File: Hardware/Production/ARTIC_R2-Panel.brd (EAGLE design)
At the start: 113 x 122.2 mm, 1045 parts, among them J1 U.FL, J10 U.FL, J11 THING_PLUS, J12 U.FL, J13 THING_PLUS, J14 U.FL, J15 THING_PLUS, J16 U.FL, J2 THING_PLUS, J3 THING_PLUS, J4 U.FL, J5 THING_PLUS, J6 U.FL, J7 THING_PLUS, J8 U.FL, J9 THING_PLUS, Q1 20V/4.2A/52mΩ/1.4W, Q2 20V/4.2A/52mΩ/1.4W, Q3 20V/4.2A/52mΩ/1.4W, Q4 20V/4.2A/52mΩ/1.4W, Q5 20V/4.2A/52mΩ/1.4W, Q6 20V/4.2A/52mΩ/1.4W, Q7 20V/4.2A/52mΩ/1.4W, Q8 20V/4.2A/52mΩ/1.4W, U1 32M SPI Flash, U10 1.8V/100mA, U11 32M SPI Flash, U12 DUAL-OPTOISOLATOR_SOIC8, U13 ARTIC_R2, U14 RFPA0133, U15 AS179-92LF, U16 1.8V/100mA, U17 32M SPI Flash, U18 DUAL-OPTOISOLATOR_SOIC8, U19 ARTIC_R2, U2 1.8V/100mA, U20 RFPA0133, U21 AS179-92LF, U22 1.8V/100mA, U23 32M SPI Flash, U24 DUAL-OPTOISOLATOR_SOIC8, U25 ARTIC_R2, U26 RFPA0133, U27 AS179-92LF, U28 1.8V/100mA, U29 32M SPI Flash, U3 ARTIC_R2, U30 DUAL-OPTOISOLATOR_SOIC8, U31 ARTIC_R2, U32 RFPA0133, U33 AS179-92LF, U34 1.8V/100mA, U35 32M SPI Flash, U36 DUAL-OPTOISOLATOR_SOIC8, U37 ARTIC_R2, U38 RFPA0133, U39 AS179-92LF, U4 RFPA0133, U40 1.8V/100mA, U41 32M SPI Flash, U42 DUAL-OPTOISOLATOR_SOIC8, U43 ARTIC_R2, U44 RFPA0133, U45 AS179-92LF, U46 1.8V/100mA, U47 32M SPI Flash, U48 DUAL-OPTOISOLATOR_SOIC8, U5 AS179-92LF, U6 DUAL-OPTOISOLATOR_SOIC8, U7 ARTIC_R2, U8 RFPA0133, U9 AS179-92LF, X1 CRYSTAL-TCXO-26MHZ, X2 CRYSTAL-TCXO-26MHZ, X3 CRYSTAL-TCXO-26MHZ, X4 CRYSTAL-TCXO-26MHZ, X5 CRYSTAL-TCXO-26MHZ, X6 CRYSTAL-TCXO-26MHZ, X7 CRYSTAL-TCXO-26MHZ, X8 CRYSTAL-TCXO-26MHZ

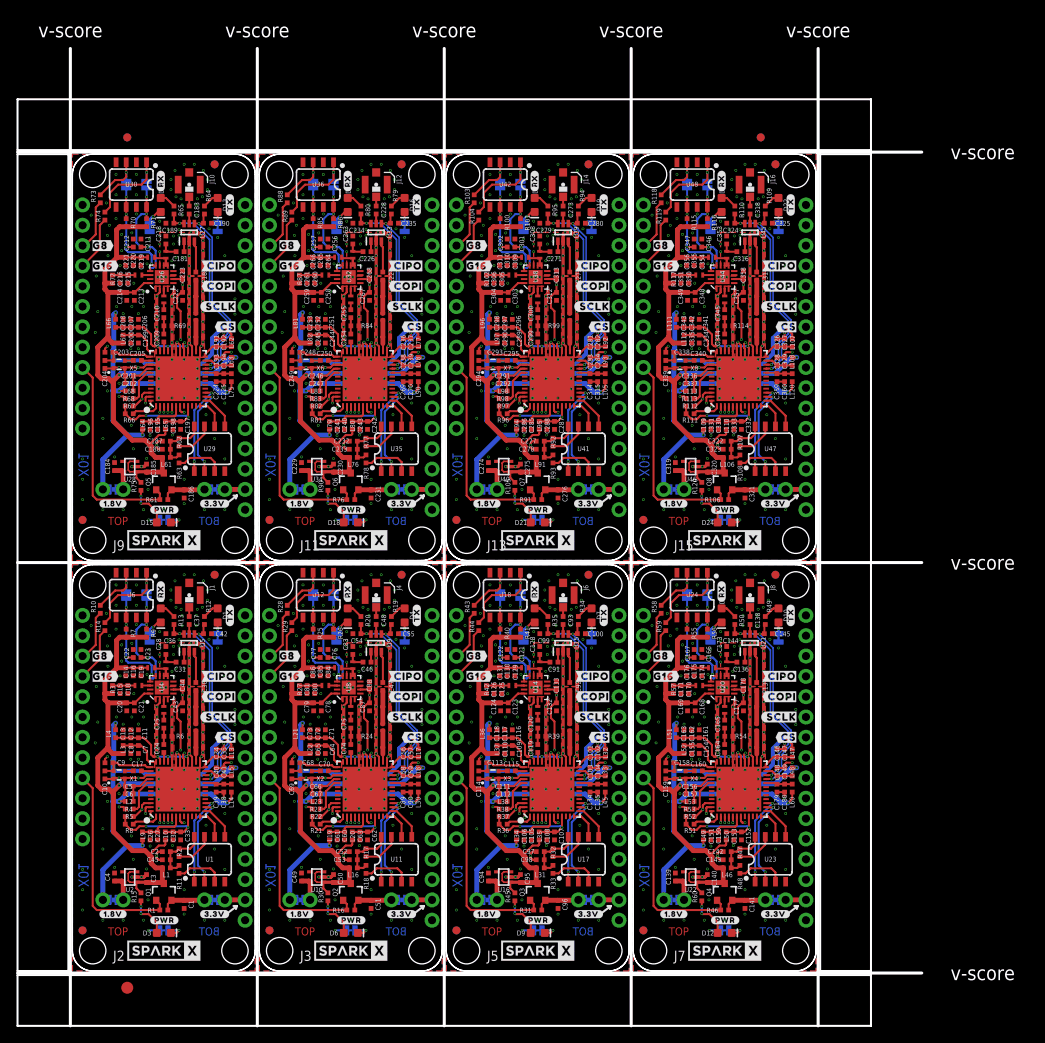
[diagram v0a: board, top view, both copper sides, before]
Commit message: ).8mm PCB with Impedance Control
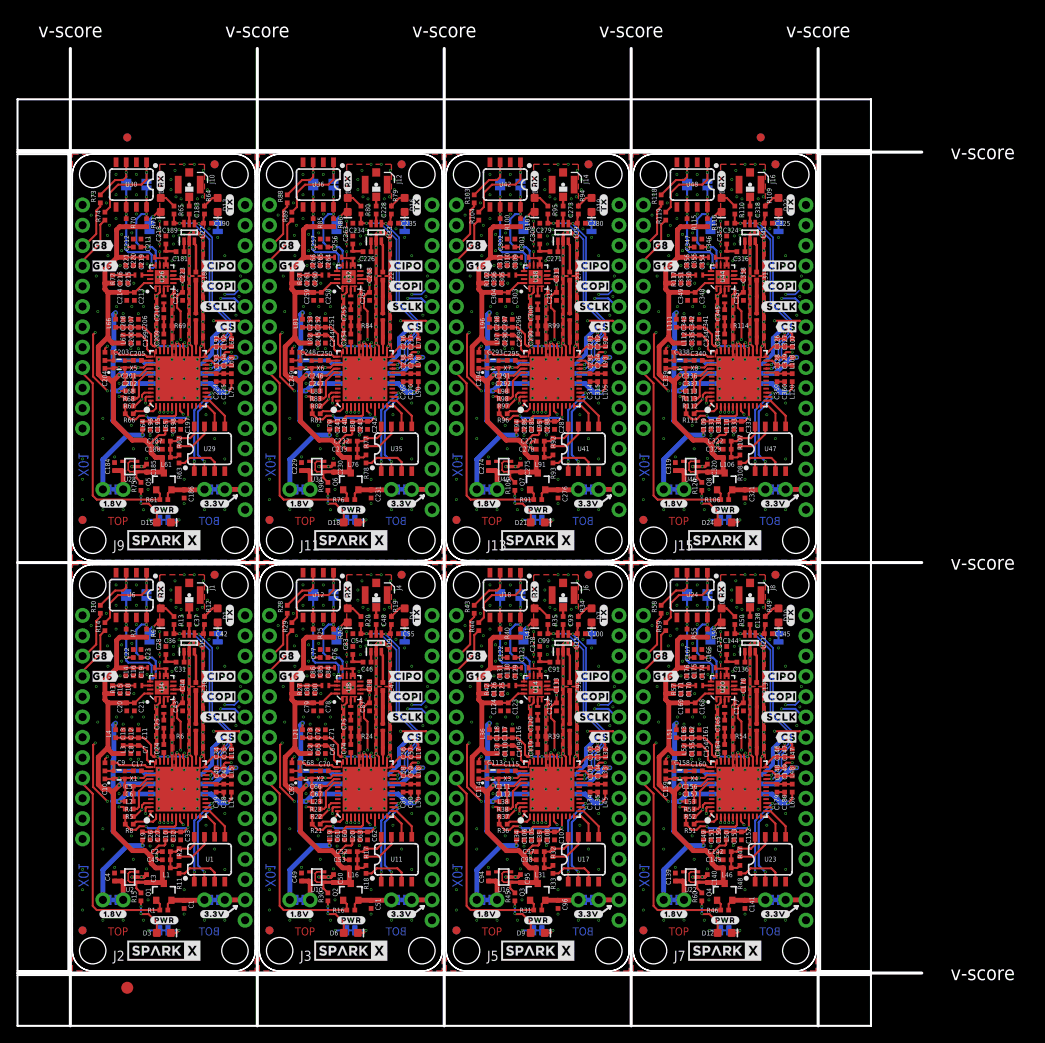
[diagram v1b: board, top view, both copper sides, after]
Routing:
- net GND7: track 79.4 -> 87.5 mm, vias 167 -> 171
- net GND6: track 79.4 -> 87.5 mm, vias 167 -> 171
- net GND5: track 79.4 -> 87.5 mm, vias 167 -> 171
- net GND2: track 79.4 -> 87.5 mm, vias 167 -> 171
- net GND1: track 79.4 -> 87.5 mm, vias 167 -> 171
- net GND3: track 79.4 -> 87.5 mm, vias 167 -> 171
- net GND4: track 79.4 -> 87.5 mm, vias 167 -> 171
- net GND: track 79.4 -> 87.5 mm, vias 167 -> 171
- net SCLK3: track 21.4 -> 24.0 mm, vias 1 -> 2
- net SCLK7: track 21.4 -> 24.0 mm, vias 1 -> 2
- net SCLK5: track 21.4 -> 24.0 mm, vias 1 -> 2
- net SCLK2: track 21.4 -> 24.0 mm, vias 1 -> 2
- net SCLK6: track 21.4 -> 24.0 mm, vias 1 -> 2
- net SCLK4: track 21.4 -> 24.0 mm, vias 1 -> 2
- net SCLK1: track 21.4 -> 24.0 mm, vias 1 -> 2
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
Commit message: Updates for X02
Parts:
- removed JP41, JP42, JP48, JP49, JP55, JP56: JUMPER-SMT_2_NO_SILK, SparkFun-Jumpers:SMT-JUMPER_2_NO_SILK
- removed JP43, JP44, JP50, JP51: JUMPER-COMBO_2_NC_TRACE, SparkFun-Jumpers:COMBO-JUMPER_2_NC_TRACE
- removed JP45, JP46, JP47, JP52, JP53, JP54: JUMPER-SMT_2_NC_TRACE_SILK, SparkFun-Jumpers:SMT-JUMPER_2_NC_TRACE_SILK
- removed U$225: (no value), output:#RESETB0
- removed U$226: (no value), output:#PWR_EN0
- removed U$227: (no value), output:GND#0
- removed U$228: (no value), output:#INT20
- removed U$229: (no value), output:#INT10
- removed U$230: (no value), output:#PWR_LED#0
- removed U$231: (no value), output:#PWR#0
- removed U$232: (no value), output:ARTIC_R2_BREAKOUT0
- added C361: 1.0nF, SparkFun-Capacitors:0402-TIGHT
- added C362, C365, C366, C367, C368, C369, C375, C378: 100pF, SparkFun-Capacitors:0402-TIGHT
- added C363: 1.0uF, SparkFun-Capacitors:0402-TIGHT
- added C364, C377: 10uF, SparkFun-Capacitors:0402-TIGHT
- added C370, C372, C376, C379, C382, C383: 2.2uF, SparkFun-Capacitors:0402-TIGHT
- added C371, C380: 22pF, SparkFun-Capacitors:0402-TIGHT
- added C373: 2.4 pF, SparkFun-Capacitors:0402_MURATA
- added C374: 9.1pF, New_Parts_Capacitors:0402-TIGHT
- added C381, C384: 0.1uF, SparkFun-Capacitors:0402-TIGHT
- added D25, D30, D35, D40: 1A/23V/620mV, SparkFun-DiscreteSemi:SOD-323
- added D26, D27, D31, D32, D36, D37: Yellow, SparkFun-LED:LED-0603
- added D28, D29, D33, D34, D38, D39: RED, SparkFun-LED:LED-0603
- added E$6: (no value), SparkFun-Retired:FIDUCIAL-1.5X3
- added J17, J20, J23: U.FL, SparkFun-Connectors:U.FL
- added J18, J21, J24: Flash Programming, SparkFun-Connectors:2X3_TEST_POINTS
- added J19, J22: THING_PLUS, New_Parts_Boards:THING_PLUS
- added K1, K2, K3, K4, K5, K6, K7, K8: TLP3475R, New_Parts_DiscreteSemi:TLP3475RTPF
- added LOGO1, LOGO10, LOGO11, LOGO12, LOGO13, LOGO14, LOGO15, LOGO16, LOGO2, LOGO3, LOGO4, LOGO5, LOGO6, LOGO7, LOGO8, LOGO9: OSHW-LOGOS, SparkFun-Aesthetics:OSHW-LOGO-S
- added TP1, TP10, TP11, TP12, TP13, TP14, TP15, TP16, TP17, TP18, TP19, TP2, TP20, TP21, TP22, TP23, TP24, TP3, TP4, TP5, TP6, TP7, TP8, TP9: TEST-POINTTP_15TH_THRU, SparkFun-Connectors:TP_15TH
- added U49, U55, U56: 3.3V, SparkFun-IC-Power:SOT23-5
- added U50: ARTIC_R2, New_Parts_IC-Comms:QFN-48
- added U51: RFPA0133, New_Parts_IC-Comms:QFN50P300X300X86-17N
- added U52: AS179-92LF, New_Parts_IC-Comms:SOT65P220X100-6N
- added U53: 1.8V/100mA, SparkFun-IC-Power:SC70
- added U54: 2Mbit SPI Flash, New_Parts_IC-Memory:SO08
- C1, C276: value 10uF -> 2.2uF
- C100, C119, C123, C167, C219, C267, C341, C71, C75: value 100pF -> 1.0uF
- C101, C148, C197, C215, C244, C359, C52: value 22pF -> 1.0uF
- C102, C143, C180, C198, C239, C286, C331, C335: value 0.1uF -> 2.2uF
- C105, C125, C146, C154, C170, C193, C195, C201, C224, C242, C269, C289, C291, C314, C330, C58, C80, C97: value 22pF -> 100pF
- C106, C135, C147, C153, C194, C202, C225, C241, C243, C270, C282, C290, C327, C337, C57, C90, C98: value 0.1uF -> 100pF
- C113, C117, C140, C203, C207, C275: value 1.0uF -> 22pF
- C114, C204: value 47nF -> 0.1uF
- C115, C205, C295: value 1.0nF -> 22pF
- C116, C144, C164, C166, C189, C206, C210, C212, C254, C256, C258, C296, C300, C302, C344, C348, C354, C48, C93: value 100pF -> 0.1uF
- C118, C141, C208, C356, C96: value 10uF -> 0.1uF
- C120, C168, C264, C312: value 100pF -> 47nF
- C121: value 100pF -> 1.0nF
- C124, C220, C268: value 2.2uF -> 10uF
- C126, C175, C223, C79, C81: value 2.2uF -> 100pF
- C127: value 2.4 pF -> 100pF; device SparkFun-Capacitors:0402_MURATA -> SparkFun-Capacitors:0402-TIGHT
- C128, C173, C218: value 9.1pF -> 100pF; device New_Parts_Capacitors:0402-TIGHT -> SparkFun-Capacitors:0402-TIGHT
- C131, C163, C253, C343: value 10uF -> 22pF
- C132, C136, C190, C226, C228, C235, C280, C324, C46, C47, C54, C84, C91: value 100pF -> 2.2uF
- C133, C85: value 2.2uF -> 2.4 pF; device SparkFun-Capacitors:0402-TIGHT -> SparkFun-Capacitors:0402_MURATA
- C134, C326: value 22pF -> 9.1pF; device SparkFun-Capacitors:0402-TIGHT -> New_Parts_Capacitors:0402-TIGHT
- C137, C316, C76: value 100pF -> 10uF
- C139, C184, C274, C342, C94, C95: value 1.0uF -> 2.2uF
- C142, C150, C187, C191, C232, C238, C246, C283, C287, C322, C328, C334: value 22pF -> 2.2uF
- C149, C196, C245, C292, C315, C53: value 0.1uF -> 1.0uF
- C151, C155, C157, C188, C247, C284, C323, C59, C61, C63, C65, C67: value 0.1uF -> 22pF
- C152, C156, C240, C260, C285, C336, C350, C56, C60, C62, C64, C66: value 22pF -> 0.1uF
- C158, C162, C248, C252, C68: value 1.0uF -> 0.1uF
- C159, C69: value 47nF -> 22pF
- C160, C70: value 1.0nF -> 0.1uF
- C161, C165, C209, C211, C213, C227, C251, C255, C257, C299, C301, C303, C309, C347, C357, C55, C92: value 100pF -> 22pF
- C169, C265, C313: value 2.2uF -> 1.0nF
- C171: value 2.2uF -> 1.0uF
- C172: value 2.4 pF -> 10uF; device SparkFun-Capacitors:0402_MURATA -> SparkFun-Capacitors:0402-TIGHT
- C176, C186, C221, C231, C266, C298, C321, C51: value 10uF -> 100pF
- C181, C325: value 100pF -> 2.4 pF; device SparkFun-Capacitors:0402-TIGHT -> SparkFun-Capacitors:0402_MURATA
- C182: value 100pF -> 9.1pF; device SparkFun-Capacitors:0402-TIGHT -> New_Parts_Capacitors:0402-TIGHT
- C185: value 1.0uF -> 10uF
- C214, C304, C306, C310, C358: value 2.2uF -> 0.1uF
- C216: value 2.2uF -> 47nF
- C217: value 2.4 pF -> 1.0nF; device SparkFun-Capacitors:0402_MURATA -> SparkFun-Capacitors:0402-TIGHT
- C229: value 1.0uF -> 2.4 pF; device SparkFun-Capacitors:0402-TIGHT -> SparkFun-Capacitors:0402_MURATA
- C230: value 1.0uF -> 9.1pF; device SparkFun-Capacitors:0402-TIGHT -> New_Parts_Capacitors:0402-TIGHT
- C233, C329: value 0.1uF -> 10uF
- C249, C339: value 47nF -> 100pF
- C250: value 1.0nF -> 100pF
- C259, C261, C349, C351, C355: value 2.2uF -> 22pF
- C262, C352: value 2.4 pF -> 0.1uF; device SparkFun-Capacitors:0402_MURATA -> SparkFun-Capacitors:0402-TIGHT
- C263: value 9.1pF -> 1.0uF; device New_Parts_Capacitors:0402-TIGHT -> SparkFun-Capacitors:0402-TIGHT
- C277: value 22pF -> 2.4 pF; device SparkFun-Capacitors:0402-TIGHT -> SparkFun-Capacitors:0402_MURATA
- C278: value 0.1uF -> 9.1pF; device SparkFun-Capacitors:0402-TIGHT -> New_Parts_Capacitors:0402-TIGHT
- C281, C89: value 22pF -> 10uF
- C294: value 47nF -> 2.2uF
- C297, C319, C320, C338, C49, C50: value 1.0uF -> 100pF
- C307: value 2.4 pF -> 22pF; device SparkFun-Capacitors:0402_MURATA -> SparkFun-Capacitors:0402-TIGHT
- C308: value 9.1pF -> 0.1uF; device New_Parts_Capacitors:0402-TIGHT -> SparkFun-Capacitors:0402-TIGHT
- C311: value 10uF -> 1.0uF
- C340: value 1.0nF -> 1.0uF
- C353, C83: value 9.1pF -> 22pF; device New_Parts_Capacitors:0402-TIGHT -> SparkFun-Capacitors:0402-TIGHT
- C360: value 0.1uF -> 47nF
- C72: value 1.0uF -> 47nF
- C73: value 10uF -> 1.0nF
- C82: value 2.4 pF -> 2.2uF; device SparkFun-Capacitors:0402_MURATA -> SparkFun-Capacitors:0402-TIGHT
- C86: value 10uF -> 9.1pF; device SparkFun-Capacitors:0402-TIGHT -> New_Parts_Capacitors:0402-TIGHT
- D10, D20, D5: value Yellow -> 1A/23V/620mV; device SparkFun-LED:LED-0603 -> SparkFun-DiscreteSemi:SOD-323
- D12, D21, D6: value RED -> Yellow
- D13, D14, D19, D23, D4, D8: value Yellow -> RED
- D15: value RED -> 1A/23V/620mV; device SparkFun-LED:LED-0603 -> SparkFun-DiscreteSemi:SOD-323
- J10, J16: value U.FL -> THING_PLUS; device SparkFun-Connectors:U.FL -> New_Parts_Boards:THING_PLUS
- J11: value THING_PLUS -> U.FL; device New_Parts_Boards:THING_PLUS -> SparkFun-Connectors:U.FL
- J12, J6: value U.FL -> Flash Programming; device SparkFun-Connectors:U.FL -> SparkFun-Connectors:2X3_TEST_POINTS
- J15, J5, J9: value THING_PLUS -> Flash Programming; device New_Parts_Boards:THING_PLUS -> SparkFun-Connectors:2X3_TEST_POINTS
- JP1, JP15, JP16, JP2, JP22, JP23, JP30, JP36, JP37, JP8: value JUMPER-COMBO_2_NC_TRACE -> JUMPER-SMT_2_NC_TRACE_SILK; device SparkFun-Jumpers:COMBO-JUMPER_2_NC_TRACE -> SparkFun-Jumpers:SMT-JUMPER_2_NC_TRACE_SILK
- JP13, JP20, JP21, JP27, JP28, JP35, JP6: value JUMPER-SMT_2_NO_SILK -> JUMPER-SMT_2_NC_TRACE_SILK; device SparkFun-Jumpers:SMT-JUMPER_2_NO_SILK -> SparkFun-Jumpers:SMT-JUMPER_2_NC_TRACE_SILK
- JP19, JP24, JP39: value JUMPER-SMT_2_NC_TRACE_SILK -> JUMPER-SMT_2_NO_SILK; device SparkFun-Jumpers:SMT-JUMPER_2_NC_TRACE_SILK -> SparkFun-Jumpers:SMT-JUMPER_2_NO_SILK
- JP29, JP9: value JUMPER-COMBO_2_NC_TRACE -> JUMPER-SMT_2_NO_SILK; device SparkFun-Jumpers:COMBO-JUMPER_2_NC_TRACE -> SparkFun-Jumpers:SMT-JUMPER_2_NO_SILK
- Q1, Q2, Q3, Q4, Q5, Q6, Q7, Q8: value 20V/4.2A/52mΩ/1.4W -> 3.1A/30V/105mΩ
- R10, R103, R105, R118, R120, R14, R28, R30, R43, R45, R58, R60, R73, R75, R88, R90: value 1k -> 100k
- R100, R115, R25, R40, R55, R7, R70, R85: value 100k -> 10k
- R101, R116, R26, R41, R56, R71, R86: value 100k -> 3.9OHM; device SparkFun-Resistors:0402-TIGHT -> New_Parts_Resistors:0402-TIGHT
- R102, R117, R27, R42, R57, R72, R87: value 3.9OHM -> 1k; device New_Parts_Resistors:0402-TIGHT -> SparkFun-Resistors:0402-TIGHT
- R9: value 100k -> 1k
- U$100: device output:#SCLK0 -> output:GND#0
- U$101: device output:SCLK#0 -> output:#INT20
- U$102: device output:#CS0 -> output:#INT10
- U$103: device output:CS#0 -> output:#PWR_LED#0
- U$104: device output:G8#0 -> output:#PWR#0
- U$105: device output:#G80 -> output:ARTIC_R2_BREAKOUT0
- U$106: device output:G16#0 -> output:#RF_LED#0
- U$107: device output:#G160 -> output:#GAIN8#0
- U$108: device output:#BOOT0 -> output:#RF#0
- U$109: device output:#RESETB0 -> output:#RF_EN#0
- U$110: device output:#PWR_EN0 -> output:#VBATT#0
- U$111: device output:GND#0 -> output:##8DB#0
- U$112: device output:#INT20 -> output:#VUSB#0
- U$113: device output:#INT10 -> output:#RX_LED#0
- U$114: device output:#PWR_LED#0 -> output:#TX_LED#0
- U$115: device output:#PWR#0 -> output:#TX#0
- U$116: device output:ARTIC_R2_BREAKOUT0 -> output:#RX#0
- U$117: device output:#RX_LED#0 -> output:CIPO#0
- U$118: device output:#TX_LED#0 -> output:#CIPO0
- U$119, U$91: device output:#3#3V#0 -> output:#COPI0
- U$120, U$148: device output:#3#3V#0 -> output:COPI#0
- U$121, U$93: device output:#1#8V#0 -> output:#SCLK0
- U$122, U$150: device output:#1#8V#0 -> output:SCLK#0
- U$123: device output:#TX#0 -> output:#CS0
- U$124: device output:#RX#0 -> output:CS#0
- U$125: device output:CIPO#0 -> output:#BOOT0
- U$126: device output:#CIPO0 -> output:#RESETB0
- U$127: device output:#COPI0 -> output:#PWR_EN0
- U$128: device output:COPI#0 -> output:GND#0
- U$129: device output:#SCLK0 -> output:#INT20
- U$130: device output:SCLK#0 -> output:#INT10
- U$131: device output:#CS0 -> output:#PWR_LED#0
- U$132: device output:CS#0 -> output:#PWR#0
- U$133: device output:G8#0 -> output:ARTIC_R2_BREAKOUT0
- U$134: device output:#G80 -> output:#RF_LED#0
- U$135: device output:G16#0 -> output:#GAIN8#0
- U$136: device output:#G160 -> output:#RF#0
- U$137: device output:#BOOT0 -> output:#RF_EN#0
- U$138: device output:#RESETB0 -> output:#VBATT#0
- U$139: device output:#PWR_EN0 -> output:##8DB#0
- U$140: device output:GND#0 -> output:#VUSB#0
- U$141: device output:#INT20 -> output:#RX_LED#0
- U$142: device output:#INT10 -> output:#TX_LED#0
- U$143: device output:#PWR_LED#0 -> output:#TX#0
- U$144: device output:#PWR#0 -> output:#RX#0
- U$145: device output:ARTIC_R2_BREAKOUT0 -> output:CIPO#0
- U$146: device output:#RX_LED#0 -> output:#CIPO0
- U$147: device output:#TX_LED#0 -> output:#COPI0
- U$149, U$177: device output:#3#3V#0 -> output:#SCLK0
- U$151, U$179: device output:#1#8V#0 -> output:#CS0
- U$152: device output:#TX#0 -> output:CS#0
- U$153: device output:#RX#0 -> output:#BOOT0
- U$154: device output:CIPO#0 -> output:#RESETB0
- U$155: device output:#CIPO0 -> output:#PWR_EN0
- U$156: device output:#COPI0 -> output:GND#0
- U$157: device output:COPI#0 -> output:#INT20
- U$158: device output:#SCLK0 -> output:#INT10
- U$159: device output:SCLK#0 -> output:#PWR_LED#0
- U$160: device output:#CS0 -> output:#PWR#0
- U$161: device output:CS#0 -> output:ARTIC_R2_BREAKOUT0
- U$162: device output:G8#0 -> output:#RF_LED#0
- U$163: device output:#G80 -> output:#GAIN8#0
- U$164: device output:G16#0 -> output:#RF#0
- U$165: device output:#G160 -> output:#RF_EN#0
- U$166: device output:#BOOT0 -> output:#VBATT#0
- U$167: device output:#RESETB0 -> output:##8DB#0
- U$168: device output:#PWR_EN0 -> output:#VUSB#0
- U$169: device output:GND#0 -> output:#RX_LED#0
- U$170: device output:#INT20 -> output:#TX_LED#0
- U$171: device output:#INT10 -> output:#TX#0
- U$172: device output:#PWR_LED#0 -> output:#RX#0
- U$173: device output:#PWR#0 -> output:CIPO#0
- U$174: device output:ARTIC_R2_BREAKOUT0 -> output:#CIPO0
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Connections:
- removed net 3.3V: C1.1, JP1.2, JP1.4, Q1.2, R1.2
- removed net 3.3V1: C51.1, JP8.2, JP8.4, Q2.2, R16.2
- removed net 3.3V2: C96.1, JP15.2, JP15.4, Q3.2, R31.2
- removed net 3.3V3: C141.1, JP22.2, JP22.4, Q4.2, R46.2
- removed net 3.3V4: C186.1, JP29.2, JP29.4, Q5.2, R61.2
- removed net 3.3V5: C231.1, JP36.2, JP36.4, Q6.2, R76.2
- removed net 3.3V6: C276.1, JP43.2, JP43.4, Q7.2, R91.2
- removed net 3.3V7: C321.1, JP50.2, JP50.4, Q8.2, R106.2
- removed net G10: J11.4, R89.2
- removed net G11: J11.3, R88.1
- removed net G12: J13.4, R104.2
- removed net G13: J13.3, R103.1
- removed net G14: J15.4, R119.2
- removed net G15: J15.3, R118.1
- removed net G16: J2.4, R14.2
- removed net G9: J9.3, R73.1
- removed net N$265: C341.1, C342.1, C343.1, L111.1, U43.28, U43.33, U43.35
- removed net N$266: C334.1, C335.1, L112.1, U43.36
- removed net N$267: R113.1, U43.41
- removed net N$268: C336.1, C337.1, L113.1, U43.40
- removed net N$269: C338.1, C339.1, U43.37, X8.4
- removed net N$270: C340.1, X8.3
- removed net N$271: C340.2, U43.38
- removed net N$272: C344.1, U43.34
- removed net N$273: C344.2, C345.1, R114.2
- removed net N$274: L115.P$2, U44.14
- removed net N$275: C350.1, C351.1, L115.P$1, R117.1
- removed net N$276: C345.2, L114.P$1
- removed net N$277: L114.P$2, U44.3
- removed net N$278: L116.P$2, L117.P$1, U44.10, U44.9
- removed net N$279: C352.P$1, L118.P$2, U43.26
- removed net N$280: J15.27, JP50.1, JP50.3
- removed net N$281: JP56.1, R118.2, U48.3
- removed net N$282: JP55.1, R119.1, U48.1
- removed net N$283: C359.1, C360.1, L120.1, U43.20
- removed net N$284: C319.1, JP51.1, JP51.3, U46.5
- removed net N$285: D22.C, JP52.2
- removed net N$286: D23.C, JP53.2
- removed net N$287: D24.A, R120.1
- removed net N$288: D24.C, JP54.2
- removed net PWR_EN: J2.9, Q1.1, R1.1
- removed net PWR_EN1: J3.9, Q2.1, R16.1
- removed net PWR_EN2: J5.9, Q3.1, R31.1
- removed net PWR_EN3: J7.9, Q4.1, R46.1
- removed net PWR_EN4: J9.9, Q5.1, R61.1
- removed net PWR_EN5: J11.9, Q6.1, R76.1
- removed net PWR_EN6: J13.9, Q7.1, R91.1
- removed net PWR_EN7: J15.9, Q8.1, R106.1
- removed net RFG10: C256.2, JP41.2, R86.1, U32.13, U36.8
- removed net RFG11: C257.2, JP42.2, R85.1, U32.12, U36.6
- removed net RFG12: C301.2, JP48.2, R101.1, U38.13, U42.8
- removed net RFG13: C302.2, JP49.2, R100.1, U38.12, U42.6
- removed net RFG14: C346.2, JP55.2, R116.1, U44.13, U48.8
- removed net RFG15: C347.2, JP56.2, R115.1, U44.12, U48.6
- removed net RFG16: C23.2, JP6.2, R9.1, U4.13, U6.8
- removed net RFG9: C212.2, JP35.2, R70.1, U26.12, U30.6
- new net ARTIC_PWR_EN: J2.8, R1.2, U7.3
- new net ARTIC_PWR_EN1: J3.8, R14.2, U13.3
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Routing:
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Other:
- board size 113 x 122.2 mm -> 113 x 116.3 mm
- board text added: "X02"
- board text removed: "X01"

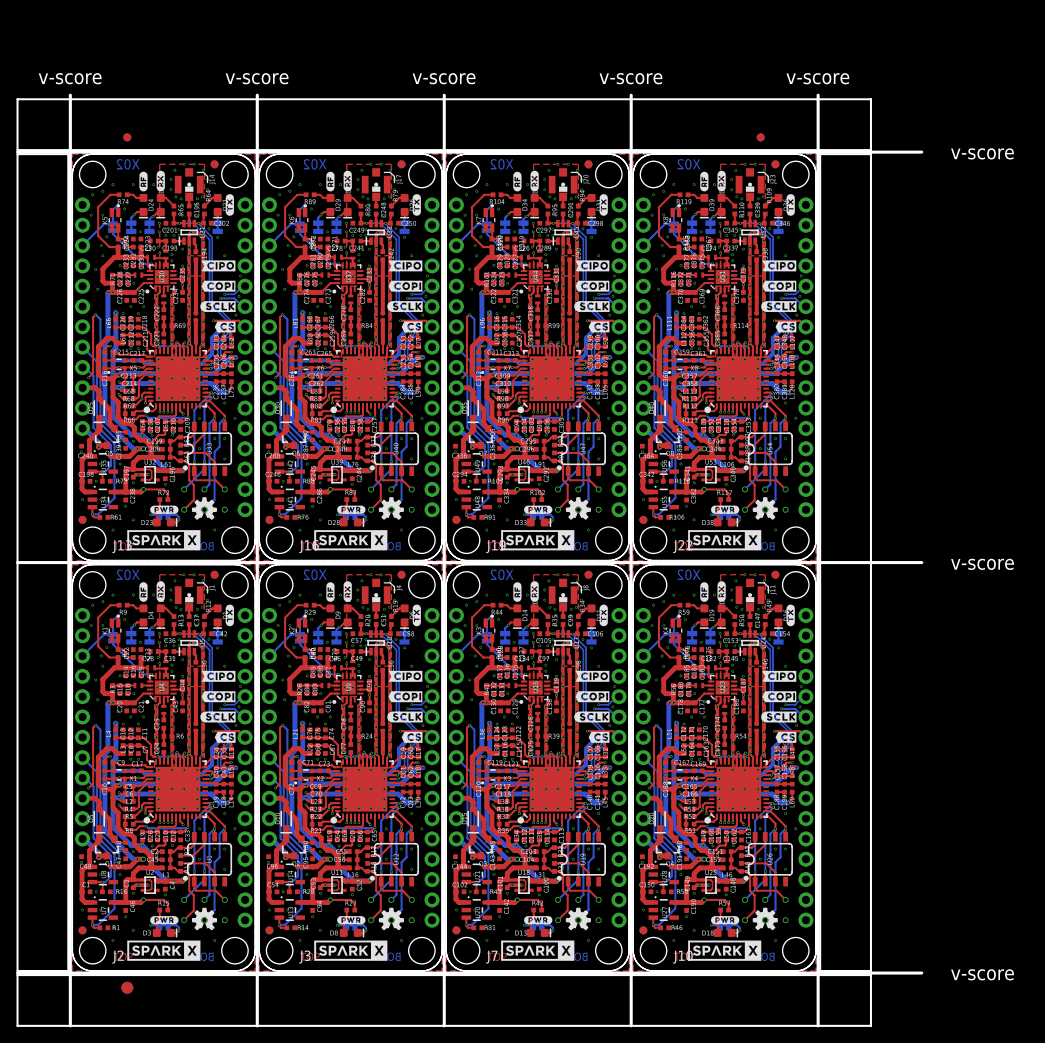
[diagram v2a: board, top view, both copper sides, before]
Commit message: Updates for X03. Design now includes a 3.0V regulator for the RF amp gain and bias.
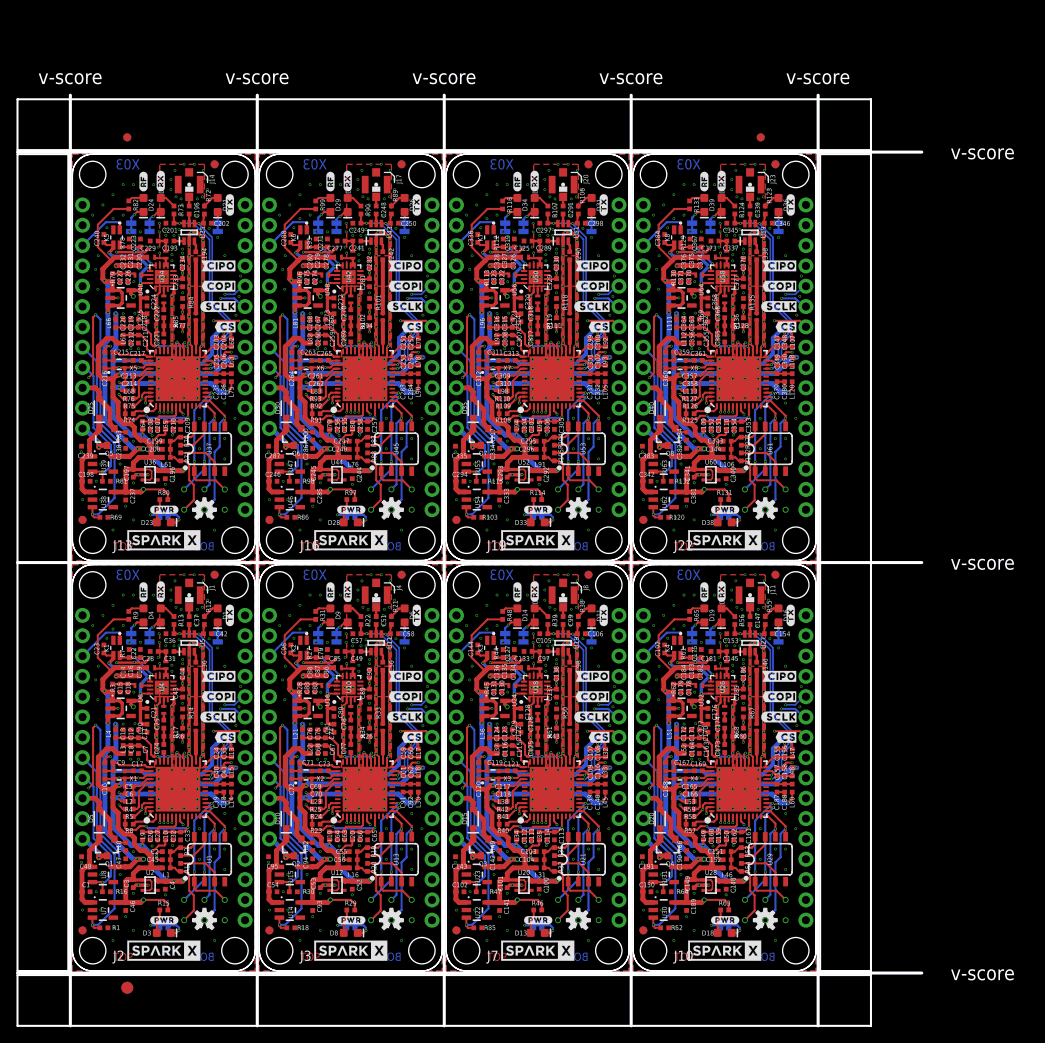
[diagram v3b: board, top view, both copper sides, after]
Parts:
- removed JP33, JP35, JP36, JP37, JP38, JP40: JUMPER-SMT_2_NC_TRACE_SILK, SparkFun-Jumpers:SMT-JUMPER_2_NC_TRACE_SILK
- removed JP34, JP39: JUMPER-SMT_2_NO_SILK, SparkFun-Jumpers:SMT-JUMPER_2_NO_SILK
- removed U$217: (no value), output:ARTIC_R2_BREAKOUT0
- removed U$218: (no value), output:#RF_LED#0
- removed U$219: (no value), output:#GAIN8#0
- removed U$220: (no value), output:#RF#0
- removed U$221: (no value), output:#RF_EN#0
- removed U$222: (no value), output:#VBATT#0
- removed U$223: (no value), output:##8DB#0
- removed U$224: (no value), output:#VUSB#0
- added R121, R122: 0, SparkFun-Resistors:0402-TIGHT
- added R123, R124, R131, R133: 1k, SparkFun-Resistors:0402-TIGHT
- added R125, R126, R134: 100k, SparkFun-Resistors:0402-TIGHT
- added R127: 33k, SparkFun-Resistors:0402-TIGHT
- added R128: 220OHM, New_Parts_Resistors:0402-TIGHT
- added R129, R132: 10k, SparkFun-Resistors:0402-TIGHT
- added R130: 3.9OHM, New_Parts_Resistors:0402-TIGHT
- added R135: 470, New_Parts_Resistors:0402-TIGHT
- added R136: 47, New_Parts_Resistors:0402-TIGHT
- added TP25, TP26, TP27, TP28, TP29, TP30, TP31, TP32: TEST-POINTTP_15TH_THRU, SparkFun-Connectors:TP_15TH
- added U57: ARTIC_R2, New_Parts_IC-Comms:QFN-48
- added U58: RFPA0133, New_Parts_IC-Comms:QFN50P300X300X86-17N
- added U59: AS179-92LF, New_Parts_IC-Comms:SOT65P220X100-6N
- added U60: 1.8V/100mA, SparkFun-IC-Power:SC70
- added U61: 2Mbit SPI Flash, New_Parts_IC-Memory:SO08
- added U62, U63: 3.3V, SparkFun-IC-Power:SOT23-5
- added U64: 3.0V, New_Parts_IC-Power:SOT23-5
- C129, C135, C138, C177, C183, C186, C225, C231, C234, C273, C279, C282, C321, C327, C330, C369, C375, C378, C81, C87, C90: value 100pF -> 2.2uF
- C130, C139, C178, C187, C226, C235, C274, C283, C322, C331, C370, C379, C82, C91: value 2.2uF -> 22pF
- C131, C179, C227, C275, C323, C371, C83: value 22pF -> 2.2uF
- C132, C180, C228, C276, C324, C372, C84: value 2.2uF -> 2.4 pF; device SparkFun-Capacitors:0402-TIGHT -> SparkFun-Capacitors:0402_MURATA
- C133, C181, C229, C277, C325, C373, C85: value 2.4 pF -> 9.1pF; device SparkFun-Capacitors:0402_MURATA -> New_Parts_Capacitors:0402-TIGHT
- C134, C182, C230, C278, C326, C374, C86: value 9.1pF -> 100pF; device New_Parts_Capacitors:0402-TIGHT -> SparkFun-Capacitors:0402-TIGHT
- C136, C184, C232, C280, C328, C376, C88: value 2.2uF -> 10uF
- C137, C185, C233, C281, C329, C377, C89: value 10uF -> 100pF
- C140, C188, C236, C284, C332, C380, C92: value 22pF -> 0.1uF
- C141, C189, C237, C285, C333, C381, C93: value 0.1uF -> 2.2uF
- C143, C191, C239, C287, C335, C383, C95: value 2.2uF -> 0.1uF
- C144, C192, C240, C288, C336, C384, C96: value 0.1uF -> 100pF
- JP14, JP19, JP24, JP29, JP7, JP9: value JUMPER-SMT_2_NO_SILK -> JUMPER-SMT_2_NC_TRACE_SILK; device SparkFun-Jumpers:SMT-JUMPER_2_NO_SILK -> SparkFun-Jumpers:SMT-JUMPER_2_NC_TRACE_SILK
- R1, R103, R112, R120, R16, R30, R52, R61, R81: value 100k -> 10k
- R100, R40: value 10k -> 100k
- R101: value 3.9OHM -> 470
- R102, R119, R34: value 1k -> 47; device SparkFun-Resistors:0402-TIGHT -> New_Parts_Resistors:0402-TIGHT
- R104, R19, R20, R87: value 1k -> 0
- R105, R36, R37, R88: value 100k -> 0
- R106, R21, R22, R31, R46, R73, R82, R90, R97: value 100k -> 1k
- R107, R48, R63: value 0 -> 1k
- R108, R32, R92: value 0 -> 100k
- R109, R117, R49, R57, R74: value 1k -> 100k
- R110, R42, R59: value 1k -> 33k
- R111, R43, R60: value 100k -> 220OHM; device SparkFun-Resistors:0402-TIGHT -> New_Parts_Resistors:0402-TIGHT
- R113: value 33k -> 3.9OHM; device SparkFun-Resistors:0402-TIGHT -> New_Parts_Resistors:0402-TIGHT
- R114, R39, R99: value 220OHM -> 1k; device New_Parts_Resistors:0402-TIGHT -> SparkFun-Resistors:0402-TIGHT
- R116, R56: value 3.9OHM -> 1k; device New_Parts_Resistors:0402-TIGHT -> SparkFun-Resistors:0402-TIGHT
- R118, R14, R67: value 100k -> 470; device SparkFun-Resistors:0402-TIGHT -> New_Parts_Resistors:0402-TIGHT
- R17: value 0 -> 47; device SparkFun-Resistors:0402-TIGHT -> New_Parts_Resistors:0402-TIGHT
- R18, R47, R78: value 0 -> 10k
- R23, R83: value 33k -> 100k
- R24: value 220OHM -> 100k; device New_Parts_Resistors:0402-TIGHT -> SparkFun-Resistors:0402-TIGHT
- R25: value 10k -> 33k
- R26: value 3.9OHM -> 220OHM
- R27, R35, R44, R64, R95: value 1k -> 10k
- R28, R45, R96: value 100k -> 3.9OHM; device SparkFun-Resistors:0402-TIGHT -> New_Parts_Resistors:0402-TIGHT
- R33: value 0 -> 470; device SparkFun-Resistors:0402-TIGHT -> New_Parts_Resistors:0402-TIGHT
- R38: value 33k -> 1k
- R41: value 3.9OHM -> 100k; device New_Parts_Resistors:0402-TIGHT -> SparkFun-Resistors:0402-TIGHT
- R50: value 1k -> 470; device SparkFun-Resistors:0402-TIGHT -> New_Parts_Resistors:0402-TIGHT
- R51: value 100k -> 47; device SparkFun-Resistors:0402-TIGHT -> New_Parts_Resistors:0402-TIGHT
- R53: value 33k -> 0
- R54: value 220OHM -> 0; device New_Parts_Resistors:0402-TIGHT -> SparkFun-Resistors:0402-TIGHT
- R55: value 10k -> 1k
- R62: value 0 -> 3.9OHM; device SparkFun-Resistors:0402-TIGHT -> New_Parts_Resistors:0402-TIGHT
- R68: value 33k -> 47; device SparkFun-Resistors:0402-TIGHT -> New_Parts_Resistors:0402-TIGHT
- R69: value 220OHM -> 10k; device New_Parts_Resistors:0402-TIGHT -> SparkFun-Resistors:0402-TIGHT
- R70: value 10k -> 0
- R71: value 3.9OHM -> 0; device New_Parts_Resistors:0402-TIGHT -> SparkFun-Resistors:0402-TIGHT
- R76: value 100k -> 33k
- R77: value 0 -> 220OHM; device SparkFun-Resistors:0402-TIGHT -> New_Parts_Resistors:0402-TIGHT
- R79: value 1k -> 3.9OHM; device SparkFun-Resistors:0402-TIGHT -> New_Parts_Resistors:0402-TIGHT
- R84: value 220OHM -> 470
- R85: value 10k -> 47; device SparkFun-Resistors:0402-TIGHT -> New_Parts_Resistors:0402-TIGHT
- R86: value 3.9OHM -> 10k; device New_Parts_Resistors:0402-TIGHT -> SparkFun-Resistors:0402-TIGHT
- R93: value 0 -> 33k
- R94: value 1k -> 220OHM; device SparkFun-Resistors:0402-TIGHT -> New_Parts_Resistors:0402-TIGHT
- R98: value 33k -> 10k
- U$100: device output:GND#0 -> output:#PWR_LED#0
- U$101: device output:#INT20 -> output:#PWR#0
- U$102: device output:#INT10 -> output:ARTIC_R2_BREAKOUT0
- U$103: device output:#PWR_LED#0 -> output:#RF_LED#0
- U$104: device output:#PWR#0 -> output:#RF#0
- U$105: device output:ARTIC_R2_BREAKOUT0 -> output:#RF_EN#0
- U$106: device output:#RF_LED#0 -> output:#VBATT#0
- U$107: device output:#GAIN8#0 -> output:#VUSB#0
- U$108: device output:#RF#0 -> output:#8DB#0
- U$109: device output:#RF_EN#0 -> output:#RX_LED#0
- U$110: device output:#VBATT#0 -> output:#TX_LED#0
- U$111: device output:##8DB#0 -> output:#TX#0
- U$112: device output:#VUSB#0 -> output:#RX#0
- U$113: device output:#RX_LED#0 -> output:CIPO#0
- U$114: device output:#TX_LED#0 -> output:#CIPO0
- U$115: device output:#TX#0 -> output:#COPI0
- U$116: device output:#RX#0 -> output:COPI#0
- U$117: device output:CIPO#0 -> output:#SCLK0
- U$118: device output:#CIPO0 -> output:SCLK#0
- U$119: device output:#COPI0 -> output:#CS0
- U$120: device output:COPI#0 -> output:CS#0
- U$121: device output:#SCLK0 -> output:#BOOT0
- U$122: device output:SCLK#0 -> output:#RESETB0
- U$123: device output:#CS0 -> output:#PWR_EN0
- U$124: device output:CS#0 -> output:GND#0
- U$125: device output:#BOOT0 -> output:#INT20
- U$126: device output:#RESETB0 -> output:#INT10
- U$127: device output:#PWR_EN0 -> output:#PWR_LED#0
- U$128: device output:GND#0 -> output:#PWR#0
- U$129: device output:#INT20 -> output:ARTIC_R2_BREAKOUT0
- U$130: device output:#INT10 -> output:#RF_LED#0
- U$131: device output:#PWR_LED#0 -> output:#RF#0
- U$132: device output:#PWR#0 -> output:#RF_EN#0
- U$133: device output:ARTIC_R2_BREAKOUT0 -> output:#VBATT#0
- U$134: device output:#RF_LED#0 -> output:#VUSB#0
- U$135, U$6: device output:#GAIN8#0 -> output:#8DB#0
- U$136: device output:#RF#0 -> output:#RX_LED#0
- U$137: device output:#RF_EN#0 -> output:#TX_LED#0
- U$138: device output:#VBATT#0 -> output:#TX#0
- U$139: device output:##8DB#0 -> output:#RX#0
- U$140: device output:#VUSB#0 -> output:CIPO#0
- U$141: device output:#RX_LED#0 -> output:#CIPO0
- U$142: device output:#TX_LED#0 -> output:#COPI0
- U$143: device output:#TX#0 -> output:COPI#0
- U$144: device output:#RX#0 -> output:#SCLK0
- U$145: device output:CIPO#0 -> output:SCLK#0
- U$146: device output:#CIPO0 -> output:#CS0
- U$147: device output:#COPI0 -> output:CS#0
- U$148: device output:COPI#0 -> output:#BOOT0
- U$149: device output:#SCLK0 -> output:#RESETB0
- U$150: device output:SCLK#0 -> output:#PWR_EN0
- U$151: device output:#CS0 -> output:GND#0
- U$152: device output:CS#0 -> output:#INT20
- U$153: device output:#BOOT0 -> output:#INT10
- U$154: device output:#RESETB0 -> output:#PWR_LED#0
- U$155: device output:#PWR_EN0 -> output:#PWR#0
- U$156: device output:GND#0 -> output:ARTIC_R2_BREAKOUT0
- U$157: device output:#INT20 -> output:#RF_LED#0
- U$158: device output:#INT10 -> output:#RF#0
- U$159: device output:#PWR_LED#0 -> output:#RF_EN#0
- U$160: device output:#PWR#0 -> output:#VBATT#0
- U$161: device output:ARTIC_R2_BREAKOUT0 -> output:#VUSB#0
- U$162: device output:#RF_LED#0 -> output:#8DB#0
- U$163: device output:#GAIN8#0 -> output:#RX_LED#0
- U$164: device output:#RF#0 -> output:#TX_LED#0
- U$165: device output:#RF_EN#0 -> output:#TX#0
- U$166: device output:#VBATT#0 -> output:#RX#0
- U$167: device output:##8DB#0 -> output:CIPO#0
- U$168: device output:#VUSB#0 -> output:#CIPO0
- U$169: device output:#RX_LED#0 -> output:#COPI0
- U$170: device output:#TX_LED#0 -> output:COPI#0
- U$171: device output:#TX#0 -> output:#SCLK0
- U$172: device output:#RX#0 -> output:SCLK#0
- U$173: device output:CIPO#0 -> output:#CS0
- U$174: device output:#CIPO0 -> output:CS#0
- U$175: device output:#COPI0 -> output:#BOOT0
- U$176: device output:COPI#0 -> output:#RESETB0
- U$177: device output:#SCLK0 -> output:#PWR_EN0
- U$178: device output:SCLK#0 -> output:GND#0
- U$179: device output:#CS0 -> output:#INT20
- U$180: device output:CS#0 -> output:#INT10
- U$181: device output:#BOOT0 -> output:#PWR_LED#0
- U$182: device output:#RESETB0 -> output:#PWR#0
- U$183: device output:#PWR_EN0 -> output:ARTIC_R2_BREAKOUT0
- U$184: device output:GND#0 -> output:#RF_LED#0
- U$185: device output:#INT20 -> output:#RF#0
- U$186: device output:#INT10 -> output:#RF_EN#0
- U$187: device output:#PWR_LED#0 -> output:#VBATT#0
- U$188: device output:#PWR#0 -> output:#VUSB#0
- U$189: device output:ARTIC_R2_BREAKOUT0 -> output:#8DB#0
- U$190: device output:#RF_LED#0 -> output:#RX_LED#0
- U$191: device output:#GAIN8#0 -> output:#TX_LED#0
- U$192: device output:#RF#0 -> output:#TX#0
- U$193: device output:#RF_EN#0 -> output:#RX#0
- U$194: device output:#VBATT#0 -> output:CIPO#0
- U$195: device output:##8DB#0 -> output:#CIPO0
- U$196: device output:#VUSB#0 -> output:#COPI0
- U$197: device output:#RX_LED#0 -> output:COPI#0
- U$198: device output:#TX_LED#0 -> output:#SCLK0
- U$199: device output:#TX#0 -> output:SCLK#0
- U$200: device output:#RX#0 -> output:#CS0
- U$201: device output:CIPO#0 -> output:CS#0
- U$202: device output:#CIPO0 -> output:#BOOT0
- U$203: device output:#COPI0 -> output:#RESETB0
- U$204: device output:COPI#0 -> output:#PWR_EN0
- U$205: device output:#SCLK0 -> output:GND#0
- U$206: device output:SCLK#0 -> output:#INT20
- U$207: device output:#CS0 -> output:#INT10
- U$208: device output:CS#0 -> output:#PWR_LED#0
- U$209: device output:#BOOT0 -> output:#PWR#0
- U$210: device output:#RESETB0 -> output:ARTIC_R2_BREAKOUT0
- U$211: device output:#PWR_EN0 -> output:#RF_LED#0
- U$212: device output:GND#0 -> output:#RF#0
- U$213: device output:#INT20 -> output:#RF_EN#0
- U$214: device output:#INT10 -> output:#VBATT#0
- U$215: device output:#PWR_LED#0 -> output:#VUSB#0
- U$216: device output:#PWR#0 -> output:#8DB#0
- U$22, U$55: device output:##8DB#0 -> output:#RX_LED#0
- U$23: device output:#RX_LED#0 -> output:#TX_LED#0
- U$30: device output:#TX_LED#0 -> output:#TX#0
- U$31: device output:#TX#0 -> output:#RX#0
- U$32: device output:#RX#0 -> output:CIPO#0
- U$33: device output:CIPO#0 -> output:#CIPO0
- U$34: device output:#CIPO0 -> output:#COPI0
- U$35: device output:#COPI0 -> output:COPI#0
- U$36: device output:COPI#0 -> output:#SCLK0
- U$37: device output:#SCLK0 -> output:SCLK#0
- U$38: device output:SCLK#0 -> output:#CS0
- U$39: device output:#CS0 -> output:CS#0
- U$40: device output:CS#0 -> output:#BOOT0
- U$41: device output:#BOOT0 -> output:#RESETB0
- U$42: device output:#RESETB0 -> output:#PWR_EN0
- U$43: device output:#PWR_EN0 -> output:GND#0
- U$44: device output:GND#0 -> output:#INT20
- U$45: device output:#INT20 -> output:#INT10
- U$46: device output:#INT10 -> output:#PWR_LED#0
- U$47: device output:#PWR_LED#0 -> output:#PWR#0
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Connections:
- new net PD: C43.2, C44.1, R14.2, R17.2, U4.6
- new net PD1: C89.2, C90.1, R33.2, R34.2, U10.6
- new net PD2: C137.2, C138.1, R50.2, R51.2, U18.6
- new net PD3: C185.2, C186.1, R67.2, R68.2, U26.6
- new net PD4: C233.2, C234.1, R84.2, R85.2, U34.6
- new net PD5: C281.2, C282.1, R101.2, R102.2, U42.6
- new net PD6: C329.2, C330.1, R118.2, R119.2, U50.6
- new net PD7: C377.2, C378.1, R135.2, R136.2, U58.6
- new net VREF1: C20.2, C21.2, C23.1, K1.3, TP4.P$1, U4.13, U4.16, U6.5
- new net VREF2: C80.2, C81.2, C96.1, K2.3, TP8.P$1, U10.13, U10.16, U16.5
- new net VREF3: C128.2, C129.2, C144.1, K3.3, TP12.P$1, U18.13, U18.16, U24.5
- new net VREF4: C176.2, C177.2, C192.1, K4.3, TP16.P$1, U26.13, U26.16, U32.5
- new net VREF5: C224.2, C225.2, C240.1, K5.3, TP20.P$1, U34.13, U34.16, U40.5
- new net VREF6: C272.2, C273.2, C288.1, K6.3, TP24.P$1, U42.13, U42.16, U48.5
- new net VREF7: C320.2, C321.2, C336.1, K7.3, TP28.P$1, U50.13, U50.16, U56.5
- new net VREF8: C368.2, C369.2, C384.1, K8.3, TP32.P$1, U58.13, U58.16, U64.5
- net 1.8V1: now also TP7.P$1, U12.5; no longer TP6.P$1, U11.5
- net 1.8V2: now also TP11.P$1, U20.5; no longer TP9.P$1, U18.5
- net 1.8V3: now also TP15.P$1, U28.5; no longer TP12.P$1, U25.5
- net 1.8V4: now also TP19.P$1, U36.5; no longer TP15.P$1, U32.5
- net 1.8V5: now also TP23.P$1, U44.5; no longer TP18.P$1, U39.5
- net 1.8V6: now also TP27.P$1, U52.5; no longer TP21.P$1, U46.5
- net 1.8V7: now also TP31.P$1, U60.5; no longer TP24.P$1, U53.5
- net ARTIC_PWR_EN1: now also R18.2, U14.3; no longer R14.2, U13.3
- net ARTIC_PWR_EN2: now also R35.2, U22.3; no longer R31.2, U20.3
- net ARTIC_PWR_EN3: now also R52.2, U30.3; no longer R46.2, U27.3
- net ARTIC_PWR_EN4: now also R69.2, U38.3; no longer R61.2, U34.3
- net ARTIC_PWR_EN5: now also R86.2, U46.3; no longer R76.2, U41.3
- net ARTIC_PWR_EN6: now also R103.2, U54.3; no longer R91.2, U48.3
- net ARTIC_PWR_EN7: now also R120.2, U62.3; no longer R106.2, U55.3
- net BOOT1: now also R24.1, U9.46; no longer R22.1, U6.46
- net BOOT2: now also R41.1, U17.46; no longer R37.1, U15.46
- net BOOT3: now also R58.1, U25.46; no longer R52.1, U22.46
- net BOOT4: now also R75.1, U33.46; no longer R67.1, U29.46
- net BOOT5: now also R92.1, U41.46; no longer R82.1, U36.46
- net BOOT6: now also R109.1, U49.46; no longer R97.1, U43.46
- net BOOT7: now also R126.1, U57.46; no longer R112.1, U50.46
- net CIPO1: now also U9.5; no longer U6.5
- net CIPO2: now also U17.5; no longer U15.5
- net CIPO3: now also U25.5; no longer U22.5
- net CIPO4: now also U33.5; no longer U29.5
- net CIPO5: now also U41.5; no longer U36.5
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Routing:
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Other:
- board text added: "X03"
- board text removed: "X02"
